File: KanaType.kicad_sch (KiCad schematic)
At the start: 61 parts, among them J1 Conn_01x04_Socket, SW1 SW_Push, SW10 SW_Push, SW11 SW_Push, SW12 SW_Push, SW13 SW_Push, SW14 SW_Push, SW15 SW_Push, SW16 SW_Push, SW17 SW_Push, SW18 SW_Push, SW19 SW_Push, SW2 SW_Push, SW20 SW_Push, SW21 SW_Push, SW22 SW_Push, SW23 SW_Push, SW24 SW_Push, SW25 SW_Push, SW26 SW_Push, SW27 SW_Push, SW28 SW_Push, SW29 SW_Push, SW3 SW_Push, SW30 SW_Push, SW31 SW_Push, SW32 SW_Push, SW33 SW_Push, SW34 SW_Push, SW35 SW_Push, SW36 SW_Push, SW37 SW_Push, SW38 SW_Push, SW39 SW_Push, SW4 SW_Push, SW40 SW_Push, SW41 SW_Push, SW42 SW_Push, SW43 SW_Push, SW44 SW_Push, SW45 SW_Push, SW46 SW_Push, SW47 SW_Push, SW48 SW_Push, SW49 SW_Push, SW5 SW_Push, SW51 SW_Push, SW53 SW_Push, SW55 SW_Push, SW57 SW_Push, SW59 SW_Push, SW6 SW_Push, SW61 SW_Push, SW63 SW_Push, SW7 SW_Push, SW8 SW_Push, SW9 SW_Push, U1 Adafruit-Feather-RP2040

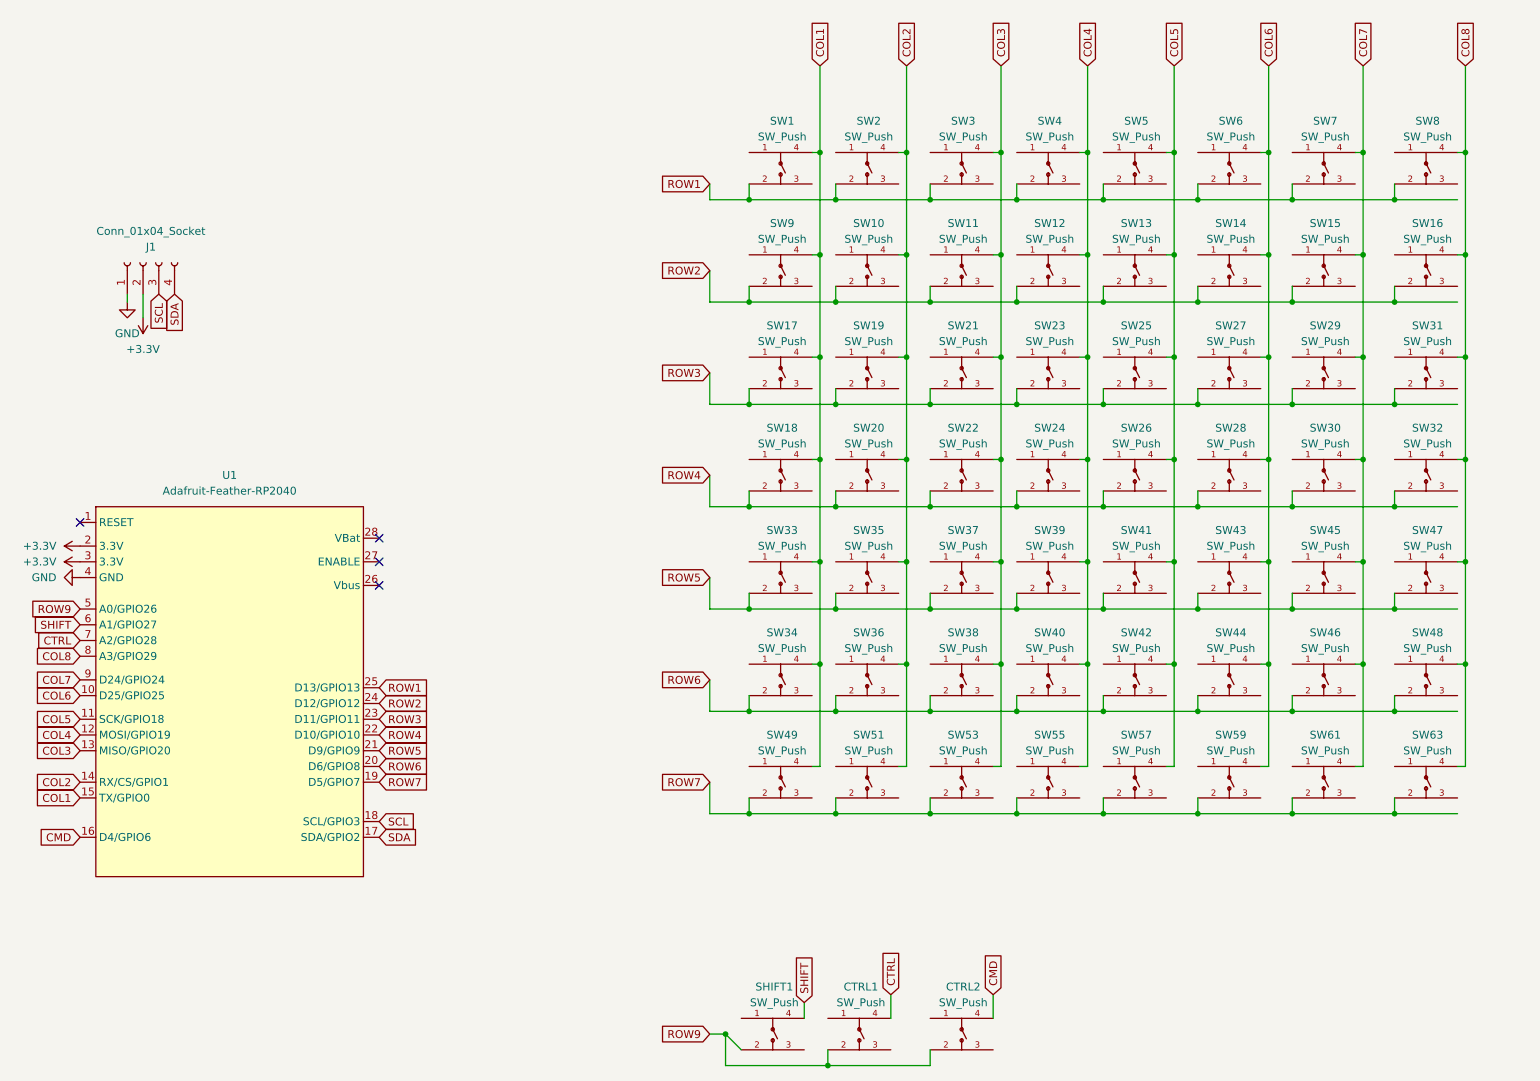
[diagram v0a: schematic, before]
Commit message: Hardware: E9 column pull-downs, OLED support parts, WAKE/RESET
- R1-R8: 8.2k pull-downs on COL1-COL8. Neutralize the RP2350-E9 erratum
  (whose internal pull-downs are unreliable) and hold the columns low when
  no key is pressed. This commits the board to ACTIVE-HIGH scanning
  permanently: columns_to_anodes=False everywhere, non-negotiable.
- R9, R10: 8.2k I2C pull-ups on SDA/SCL, so the bus is self-sufficient
  regardless of what an attached module provides.
- R11: 1k series for WAKE1, capping fault current at 3.3 mA when the key
  drives COL8 against its 8.2k pull-down.
- C1: 10 uF bulk cap across 3.3 V near J1, as the OLED transient reservoir.
- RESET1 / WAKE1 tactile switches.

Also corrects the matrix wiring: every switch now uses pad 2 -> row and
pad 4 -> column. The LCSC symbol shows diagonal internal pairing but the
YTS810SJK datasheet specifies edge pairing ({1,2} and {3,4}), and the
original pad-3 wiring shorted every key in the matrix. Caught before
fabrication.

DRC, ERC and schematic-parity were clean at the 2026-08 audit.

Co-Authored-By: Claude Opus 5 <noreply@anthropic.com>
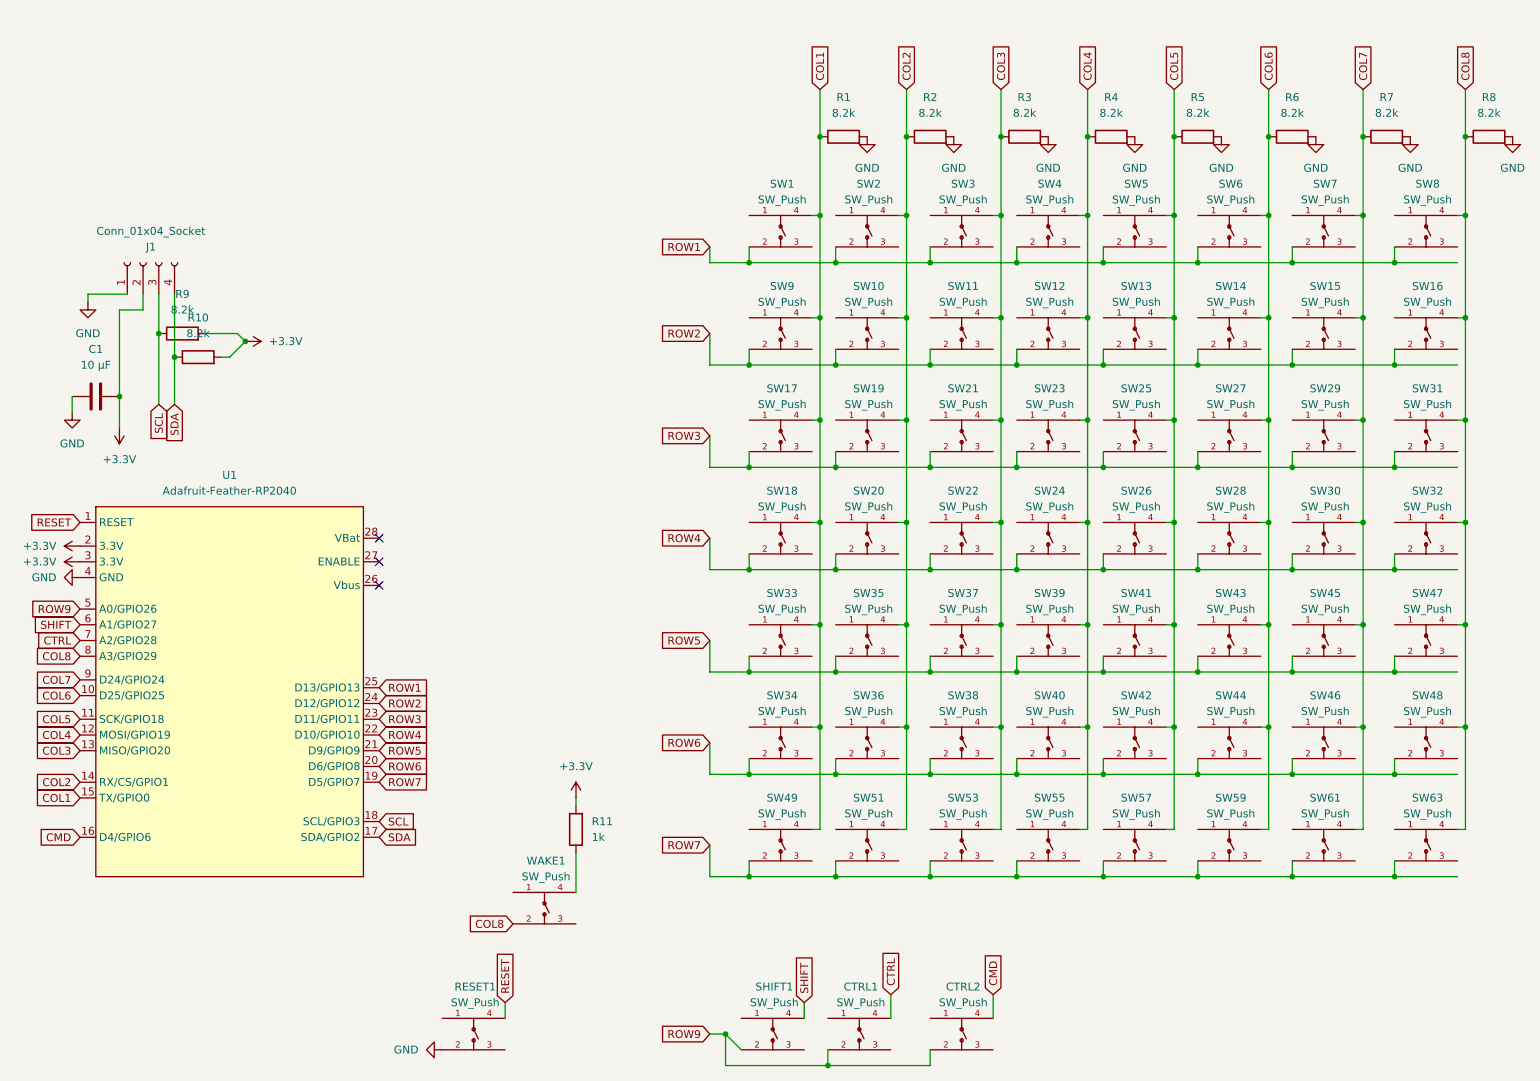
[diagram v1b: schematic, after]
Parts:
- added C1: 10 μF, Capacitor_SMD:C_0805_2012Metric_Pad1.18x1.45mm_HandSolder, symbol Device:C
- added R1, R10, R2, R3, R4, R5, R6, R7, R8, R9: 8.2k, Resistor_SMD:R_0805_2012Metric_Pad1.20x1.40mm_HandSolder, symbol Device:R
- added R11: 1k, Resistor_SMD:R_0805_2012Metric_Pad1.20x1.40mm_HandSolder, symbol Device:R
- added RESET1, WAKE1: SW_Push, LCSC:SW-SMD_4P-L4.2-W3.2-P2.15-LS4.6, symbol LCSC:YTS810SJK
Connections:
- net +3.3V: now also C1.2, R10.2, R11.2, R9.2
- net COL1: now also R1.1
- net COL2: now also R2.1
- net COL3: now also R3.1
- net COL4: now also R4.1
- net COL5: now also R5.1
- net COL6: now also R6.1
- net COL7: now also R7.1
- net COL8: now also R8.1, WAKE1.2
- net GND: now also C1.1, R1.2, R2.2, R3.2, R4.2, R5.2, R6.2, R7.2, R8.2, RESET1.2
- net SCL: now also R9.1
- net SDA: now also R10.1
- net RESET: now reaches U1.1 (RESET)
- net RESET: now also RESET1.4
- new net: R11.1, WAKE1.4
- no-connect marks 4 -> 3
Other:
- moved on the sheet: SW1, SW10, SW11, SW12, SW13, SW14, SW15, SW16, SW17, SW18, SW19, SW2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
